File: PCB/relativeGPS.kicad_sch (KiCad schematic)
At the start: 4 parts, among them SW2 EVQ-P7A01P, SW3 EVQ-P7A01P

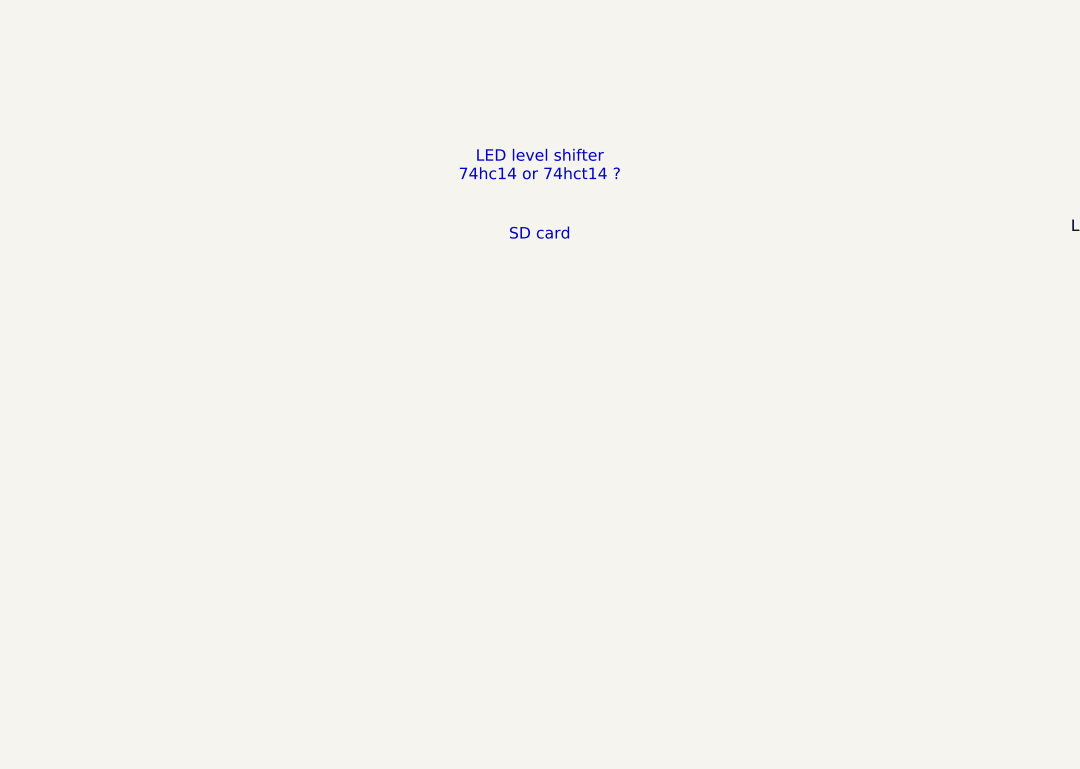
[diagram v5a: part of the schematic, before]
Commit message: Add TP & level shifter
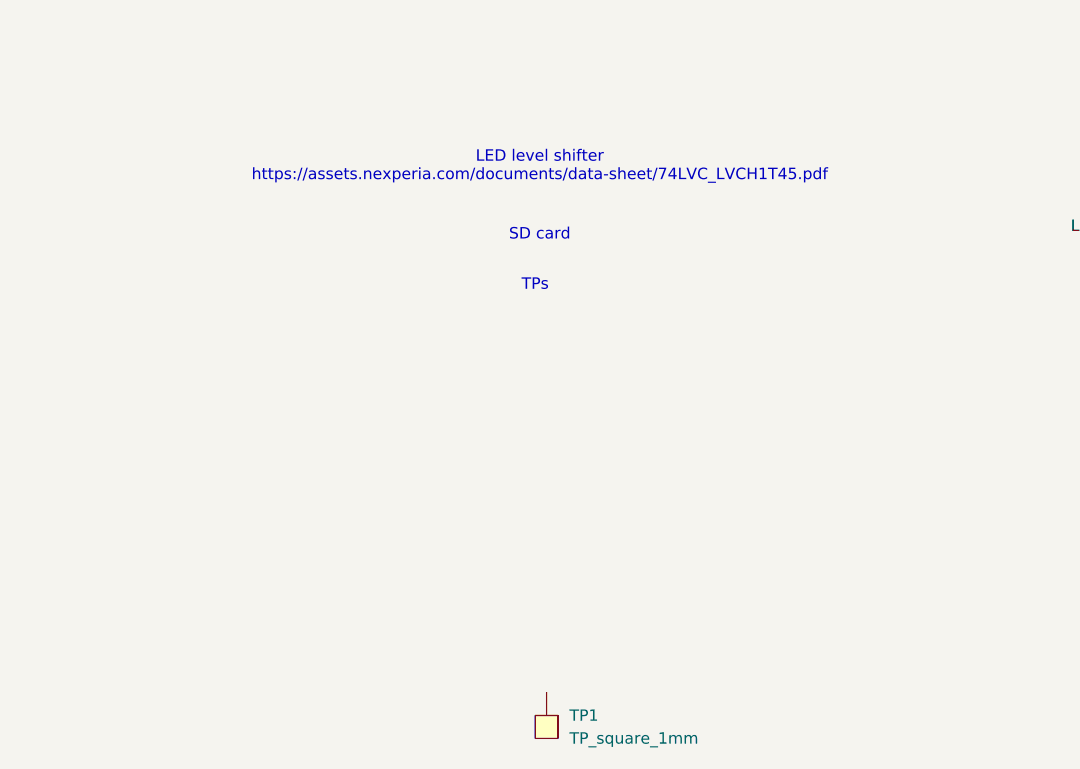
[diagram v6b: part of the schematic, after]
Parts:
- added TP1: TP_square_1mm, 011-Misc:Testpoint_square_1mm, symbol 011-Misc:Testpoint_square_1mm
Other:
- note added: "LED level shifter https://assets.nexperia.com/documents/data-sheet/74LVC_LVCH1T45.pdf"
- note added: "TPs"
- note removed: "LED level shifter 74hc14 or 74hct14 ?"
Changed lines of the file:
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@@
 		)
 	)
-	(text "LED level shifter\n74hc14 or 74hct14 ?"
+	(text "LED level shifter\nhttps://assets.nexperia.com/documents/data-sheet/74LVC_LVCH1T45.pdf"
 		(exclude_from_sim no)
 		(at 119.888 129.54 0)
@@
 		(exclude_from_sim no)
 		(at 119.888 137.16 0)
+		(effects
+			(font
+				(size 1.27 1.27)
+			)
+		)
+	)
+	(text "TPs"
+		(exclude_from_sim no)
+		(at 119.38 142.748 0)
 		(effects
 			(font
@@
 					(unit 1)
 				)
+			)
+		)
+	)
+	(symbol
+		(lib_id "011-Misc:Testpoint_square_1mm")
+		(at 120.65 191.77 270)
+		(unit 1)
+		(exclude_from_sim no)
+		(in_bom no)
+		(on_board yes)
+		(dnp no)
+		(fields_autoplaced yes)
+		(property "Reference" "TP1"
+			(at 123.19 190.4999 90)
+			(effects
+				(font
+					(size 1.27 1.27)
+				)
+				(justify left)
+			)
+		)
+		(property "Value" "TP_square_1mm"
+			(at 123.19 193.0399 90)
+			(effects
+				(font
+					(size 1.27 1.27)
+				)
+				(justify left)
+			)
+		)
+		(property "Footprint" "011-Misc:Testpoint_square_1mm"
+			(at 116.332 192.024 0)
+			(effects
+				(font
+					(size 1.27 1.27)
+				)
+				(hide yes)
+			)
+		)
+		(property "Datasheet" ""
+			(at 120.65 191.77 0)
+			(effects
+				(font
+					(size 1.27 1.27)
+				)
+				(hide yes)
+			)
+		)
+		(property "Description" ""
+			(at 120.65 191.77 0)
+			(effects
+				(font
+					(size 1.27 1.27)
+				)
+				(hide yes)
+			)
+		)
+		(pin ""
+		)
+		(instances
+			(project "relativeGPS"
+				(path "/9255e348-2f0c-48d3-8a71-46491dcb1a12"
+					(reference "TP1")
+					(unit 1)
+				)

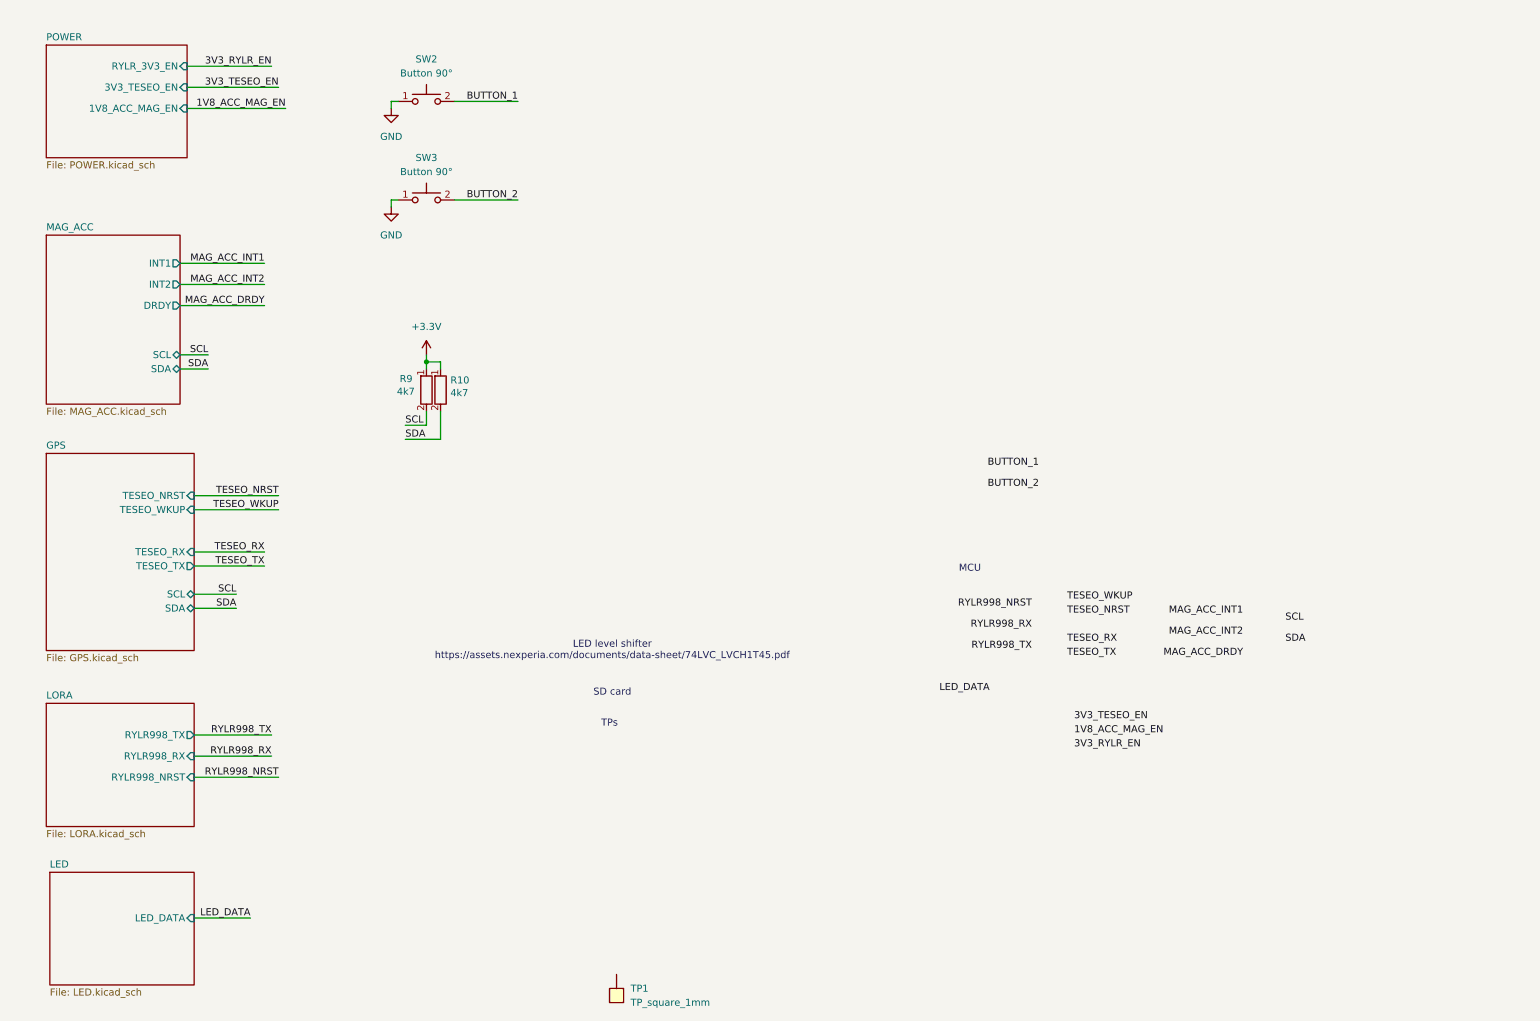
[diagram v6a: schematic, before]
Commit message: Finish schematic minus mcu
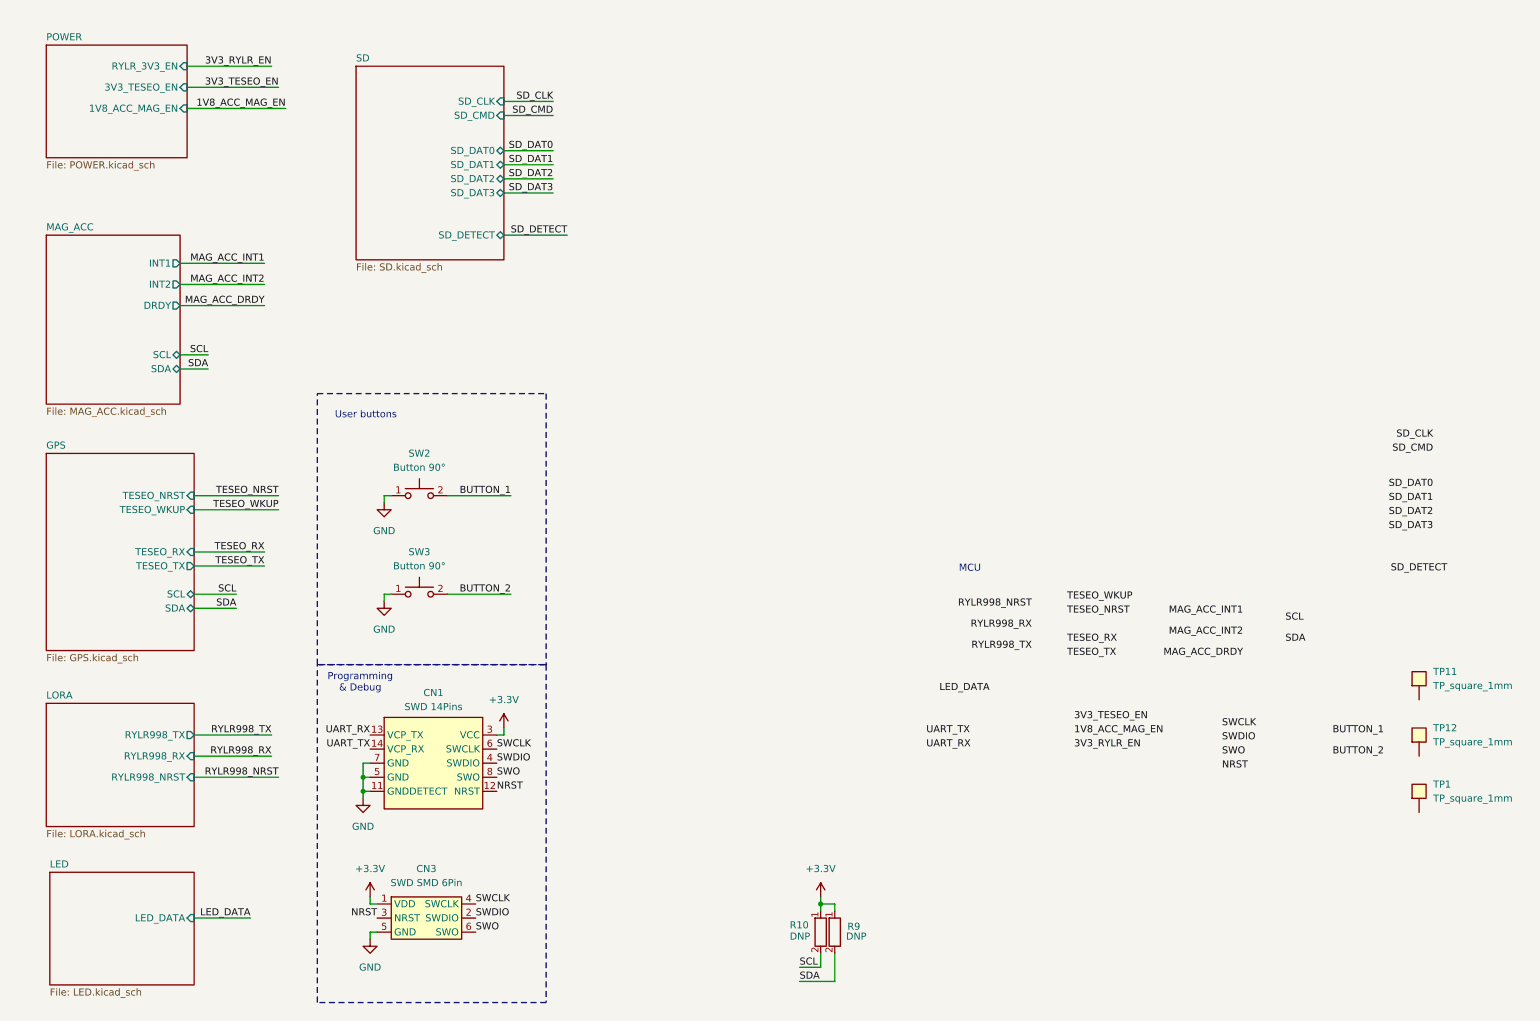
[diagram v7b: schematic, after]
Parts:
- removed R10, R9: R_4k7_1%_1/10W_0603, 001-Resistors:R_0603_H0.55, symbol 001-Resistors:R_4k7_1%_1/10W_0603
- added CN1: FTSH-107-01-L-DV-K-P-TR, 009-Connectors:FTSH-107-01-L-DV-K-P-TR, symbol 009-Connectors:Programming_SWD_14POS
- added CN3: TC2030-IDC, 009-Connectors:Debug_pads_6pin, symbol 009-Connectors:Programming_SWD_SMD_6Pin
- added R10, R9: R_DNP_0402, 001-Resistors:R_0402_H0.4, symbol 001-Resistors:R_DNP_0402
- added TP11, TP12: TP_square_1mm, 011-Misc:Testpoint_square_1mm, symbol 011-Misc:Testpoint_square_1mm
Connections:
- net +3.3V: now also CN1.3 (VCC), CN3.1 (VDD), R10.1, R9.1
- net GND: now also CN1.11 (GNDDETECT), CN1.5 (GND), CN1.7 (GND), CN3.5 (GND)
- net SCL: now also R10.2
- net SDA: now also R9.2
- new net NRST: CN1.12 (NRST), CN3.3 (NRST)
- new net SWCLK: CN1.6 (SWCLK), CN3.4 (SWCLK)
- new net SWDIO: CN1.4 (SWDIO), CN3.2 (SWDIO)
- new net SWO: CN1.8 (SWO), CN3.6 (SWO)
- new net UART_RX: CN1.13 (VCP_TX)
- new net UART_TX: CN1.14 (VCP_RX)
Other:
- added sheet SD (SD.kicad_sch)
- note added: "Programming & Debug"
- note added: "User buttons"
- note removed: "LED level shifter https://assets.nexperia.com/documents/data-sheet/74LVC_LVCH1T45.pdf"
- note removed: "SD card"
- note removed: "TPs"
- moved on the sheet: SW2, SW3, TP1

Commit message: Layout start
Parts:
- removed CN1: FTSH-107-01-L-DV-K-P-TR, 009-Connectors:FTSH-107-01-L-DV-K-P-TR, symbol 009-Connectors:Programming_SWD_14POS
- removed TP1, TP11, TP12: TP_square_1mm, 011-Misc:Testpoint_square_1mm, symbol 011-Misc:Testpoint_square_1mm
- added C17, C29, C31, C32, C33, C34, C35: C_100nF_50V_10%_X7R_0402_H0.55, 002-Capacitors:C_0402_H0.55, symbol 002-Capacitors:C_100nF_50V_10%_X7R_0402
- added C28: C_10nF_50V_10%_X7R_0402_H0.55, 002-Capacitors:C_0402_H0.55, symbol 002-Capacitors:C_10nF_50V_10%_X7R_0402
- added C36: C_10uF_10V_20%_X5R_0402_H0.55, 002-Capacitors:C_0402_H0.55, symbol 002-Capacitors:C_10uF_10V_20%_X5R_0402
- added CN1: FTSH-107-01-L-DV-K-P-TR, 009-Connectors:FTSH-107-01-L-DV-K-P-TR, symbol 009-Connectors:Programming_SWD_14Pin
- added SW4: TL3315NF160Q, 009-Connectors:TL3315NF160Q, symbol 009-Connectors:TL3315NF160Q
- added U11: STM32L431RCT6TR, 007-MCUs:LQFP-64_10x10mm_P0.5mm, symbol 007-MCUs:STM32L431RCT6TR
- added U12: ASE-8.000MHZ-L-C-T, 005-ICs:ASE-8.000MHZ-L-C-T, symbol 005-ICs:ASE-8.000MHZ-L-C-T
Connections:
- net +3.3V: now also C17.1, C28.1, C31.1, C32.1, C33.1, C34.1, C35.1, C36.1, CN1.3 (VCC), U11.1 (VBAT), U11.13 (VDDA), U11.19 (VDD), U11.32 (VDD), U11.48 (VDD), U11.64 (VDD), U12.4 (VCC)
- net BUTTON_2: now also U11.61 (PB8)
- net GND: now also C17.2, C29.2, C31.2, C32.2, C33.2, C34.2, C35.2, C36.2, CN1.11 (GNDDETECT), CN1.5 (GND), CN1.7 (GND), SW4.2, U11.12 (VSSA), U11.18 (VSS), U11.31 (VSS), U11.47 (VSS), U11.63 (VSS), U12.2 (GND)
- net LED_DATA: now also U11.36 (PB15)
- net NRST: now also C29.1, CN1.12 (NRST), SW4.1, U11.7 (NRST)
- net RYLR998_NRST: now also U11.44 (PA11)
- net RYLR998_RX: now also U11.42 (PA9)
- net RYLR998_TX: now also U11.43 (PA10)
- net SCL: now also U11.58 (PB6)
- net SDA: now also U11.59 (PB7)
- net SD_CLK: now also U11.53 (PC12)
- net SD_CMD: now also U11.54 (PD2)
- net SD_DAT0: now also U11.39 (PC8)
- net SD_DAT1: now also U11.40 (PC9)
- net SD_DAT2: now also U11.51 (PC10)
- net SD_DAT3: now also U11.52 (PC11)
- net SD_DETECT: now also U11.56 (PB4)
- net SWCLK: now also CN1.6 (SWCLK), U11.49 (PA14)
- net SWDIO: now also CN1.4 (SWDIO), U11.46 (PA13)
- net TESEO_NRST: now also U11.28 (PB2)
- net TESEO_RX: now also U11.24 (PC4)
- net TESEO_TX: now also U11.25 (PC5)
- net TESEO_WKUP: now also U11.27 (PB1)
- net UART_RX: now also CN1.13 (VCP_TX), U11.17 (PA3)
- net UART_TX: now also CN1.14 (VCP_RX), U11.16 (PA2)
- net SWO: no longer names the net of CN3.6 (SWO)
- new net: C28.2, U12.1 (STBY)
- new net: U11.5 (PH0-OSC_IN), U12.3 (Out)
- no-connect marks 0 -> 2
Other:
- note added: "vérifier rx-tx orientation for each line"
- note removed: "MCU"
